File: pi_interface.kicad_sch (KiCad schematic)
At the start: 7 parts, among them J3 GPIO, U5 M24c64

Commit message: push forwards: clock muxing, filling in blanks
Finished off the ethernet section finally.
Sorted a solution to the 25M phy clocks required for ethercat
Connected CAN as per existing hardware (and fixed a bug in speed mode)
Sorted out bypassing for MCU
Added more thoughts on the external interfaces
Started on a 24V supply
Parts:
- added JP3: KJumper_2, TestPoint:TestPoint_2Pads_Pitch2.54mm_Drill0.8mm, symbol karl-parts:KJumper_2
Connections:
- net +5V: now also JP3.2 (B); no longer J3.2 (Pin_2), J3.4 (Pin_4), TP5.1
- new net 5VPI: J3.2 (Pin_2), J3.4 (Pin_4), JP3.1 (A), TP5.1
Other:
- note added: "A "proper" power hat supplies 3/5A at 5.1. We may want to be powered by the Pi, Or attempt to power it. Just be careful ok?"
- note added: "TODO * SPI? * UART? * SWD? (you can openocd on the pi and reprogram it on the fly? heh) * Let's say a UART _at least_ ? If you do this "right", you can stack it with my of my ADC hats and get a "HWS2" without putting any analog on this board at all... ==> Doesn't even have to stack, can just have the XMC as the "base" with a pi adc on top?"
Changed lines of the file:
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@@
+		)
+	)
+	(text "TODO\n* SPI?\n* UART?\n* SWD? (you can openocd on the pi and reprogram it on the fly? heh)\n* Let's say a UART _at least_ ?\n\nIf you do this \"right\", you can stack it with my of my ADC hats and get a \"HWS2\"\nwithout putting any analog on this board at all...\n\n==> Doesn't even have to stack, can just have the XMC as the \"base\" with a pi adc on top?"
+		(exclude_from_sim no)
+		(at 82.296 123.444 0)
+		(effects
+			(font
+				(size 2.54 2.54)
+			)
+			(justify left)
+		)
+	)
+	(text "A \"proper\" power hat supplies 3/5A at 5.1.\nWe may want to be powered by the Pi,\nOr attempt to power it.  Just be careful ok?"
+		(exclude_from_sim no)
+		(at 116.586 30.48 0)
+		(effects
+			(font
+				(size 1.27 1.27)
+			)
+			(justify left)
 		)
 	)
@@
 	(wire
 		(pts
+			(xy 134.62 25.4) (xy 139.7 25.4)
+		)
+		(stroke
+			(width 0)
+			(type default)
+		)
+	)
+	(wire
+		(pts
 			(xy 63.5 73.66) (xy 66.04 73.66)
 		)
@@
 	(wire
 		(pts
-			(xy 81.28 20.32) (xy 81.28 25.4)
+			(xy 81.28 17.78) (xy 81.28 25.4)
 		)
 		(stroke
@@
 		(pts
 			(xy 40.64 50.8) (xy 66.04 50.8)
+		)
+		(stroke
+			(width 0)
+			(type default)
+		)
+	)
+	(wire
+		(pts
+			(xy 127 25.4) (xy 129.54 25.4)
 		)
 		(stroke
@@
 		)
 	)
+	(global_label "5VPI"
+		(shape bidirectional)
+		(at 81.28 17.78 0)
+		(fields_autoplaced yes)
+		(effects
+			(font
+				(size 1.27 1.27)
+			)
+			(justify left)
+		)
+		(property "Intersheetrefs" "${INTERSHEET_REFS}"
+			(at 89.5494 17.78 0)
+			(hide yes)
+			(show_name no)
+			(do_not_autoplace no)
+			(effects
+				(font
+					(size 1.27 1.27)
+				)
+				(justify left)
+			)
+		)
+	)
+	(global_label "5VPI"
+		(shape bidirectional)
+		(at 127 25.4 180)
+		(fields_autoplaced yes)
+		(effects
+			(font
+				(size 1.27 1.27)
+			)
+			(justify right)
+		)
+		(property "Intersheetrefs" "${INTERSHEET_REFS}"
+			(at 118.7306 25.4 0)
+			(hide yes)
+			(show_name no)
+			(do_not_autoplace no)
+			(effects
+				(font
+					(size 1.27 1.27)
+				)
+				(justify right)
+			)
+		)
+	)
 	(symbol
 		(lib_id "power:+5V")
-		(at 81.28 20.32 0)
+		(at 139.7 25.4 0)
 		(unit 1)
 		(body_style 1)
@@
 		(dnp no)
 		(property "Reference" "#PWR01"
-			(at 81.28 24.13 0)
+			(at 139.7 29.21 0)
 			(hide yes)
 			(show_name no)
@@
 		)
 		(property "Value" "+5V"
-			(at 81.6483 15.9956 0)
+			(at 140.0683 21.0756 0)
 			(show_name no)
 			(do_not_autoplace no)
@@
 		)
 		(property "Footprint" ""
-			(at 81.28 20.32 0)
+			(at 139.7 25.4 0)
 			(show_name no)
 			(do_not_autoplace no)
@@
 		)
 		(property "Datasheet" ""
-			(at 81.28 20.32 0)
+			(at 139.7 25.4 0)
 			(show_name no)
 			(do_not_autoplace no)
@@
 		)
 		(property "Description" "Power symbol creates a global label with name \"+5V\""
-			(at 81.28 20.32 0)
+			(at 139.7 25.4 0)
 			(hide yes)
 			(show_name no)
@@
 					(unit 1)
 				)
+			)
+		)
+	)
+	(symbol
+		(lib_id "karl-parts:KJumper_2")
+		(at 132.08 25.4 0)
+		(unit 1)
+		(body_style 1)
+		(exclude_from_sim no)
+		(in_bom yes)
+		(on_board yes)
+		(in_pos_files yes)
+		(dnp no)
+		(fields_autoplaced yes)
+		(property "Reference" "JP3"
+			(at 132.08 19.05 0)
+			(show_name no)
+			(do_not_autoplace no)
+			(effects
+				(font
+					(size 1.27 1.27)
+				)
+			)
+		)
+		(property "Value" "KJumper_2"
+			(at 132.08 21.59 0)
+			(show_name no)
+			(do_not_autoplace no)
+			(effects
+				(font
+					(size 1.27 1.27)
+				)
+			)
+		)
+		(property "Footprint" "TestPoint:TestPoint_2Pads_Pitch2.54mm_Drill0.8mm"
+			(at 132.08 25.4 0)
+			(hide yes)
+			(show_name no)
+			(do_not_autoplace no)
+			(effects
+				(font
+					(size 1.27 1.27)
+				)
+			)
+		)
+		(property "Datasheet" ""
+			(at 132.08 25.4 0)
+			(hide yes)
+			(show_name no)
+			(do_not_autoplace no)
+			(effects
+				(font
+					(size 1.27 1.27)
+				)
+			)
+		)
+		(property "Description" "Jumper, 2-pole, small symbol, open"
+			(at 132.08 25.4 0)
+			(hide yes)
+			(show_name no)
+			(do_not_autoplace no)
+			(effects
+				(font
+					(size 1.27 1.27)
+				)
+			)
+		)
+		(pin "2"
+		)
+		(pin "1"
+		)
+		(instances
+			(project "xmc-ecat-enet-twin"
+				(path "/f5c7c34d-e330-4aa5-be7e-80f0a3a977af/8a413513-9505-4930-8a63-18ba86ee9e3b"
+					(reference "JP3")
+					(unit 1)
+				)

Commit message: finish a 24V supply
went with a more modern one, plenty of room.  Should be pretty good now.
Went over and filled in a bunch of missing parts and things, cleaned up
as much as I could 0603 vs 0402 for most, updated some thigns to current
atomic part library.

still to go, the "pi" interface and some sort of spi/io interface?
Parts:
- removed C2: 100nF, Capacitor_SMD:C_0603_1608Metric, symbol karl-atomic-basic:KC0603_100nF
- added C25: 100nF, Capacitor_SMD:C_0402_1005Metric, symbol karl-atomic-basic:KC0402_100nF
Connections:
- net +3V3: now also C25.1; no longer JP1.2 (B)
- net GND: now also C25.2
- net at U5.7 (WP): no longer JP1.1 (A)

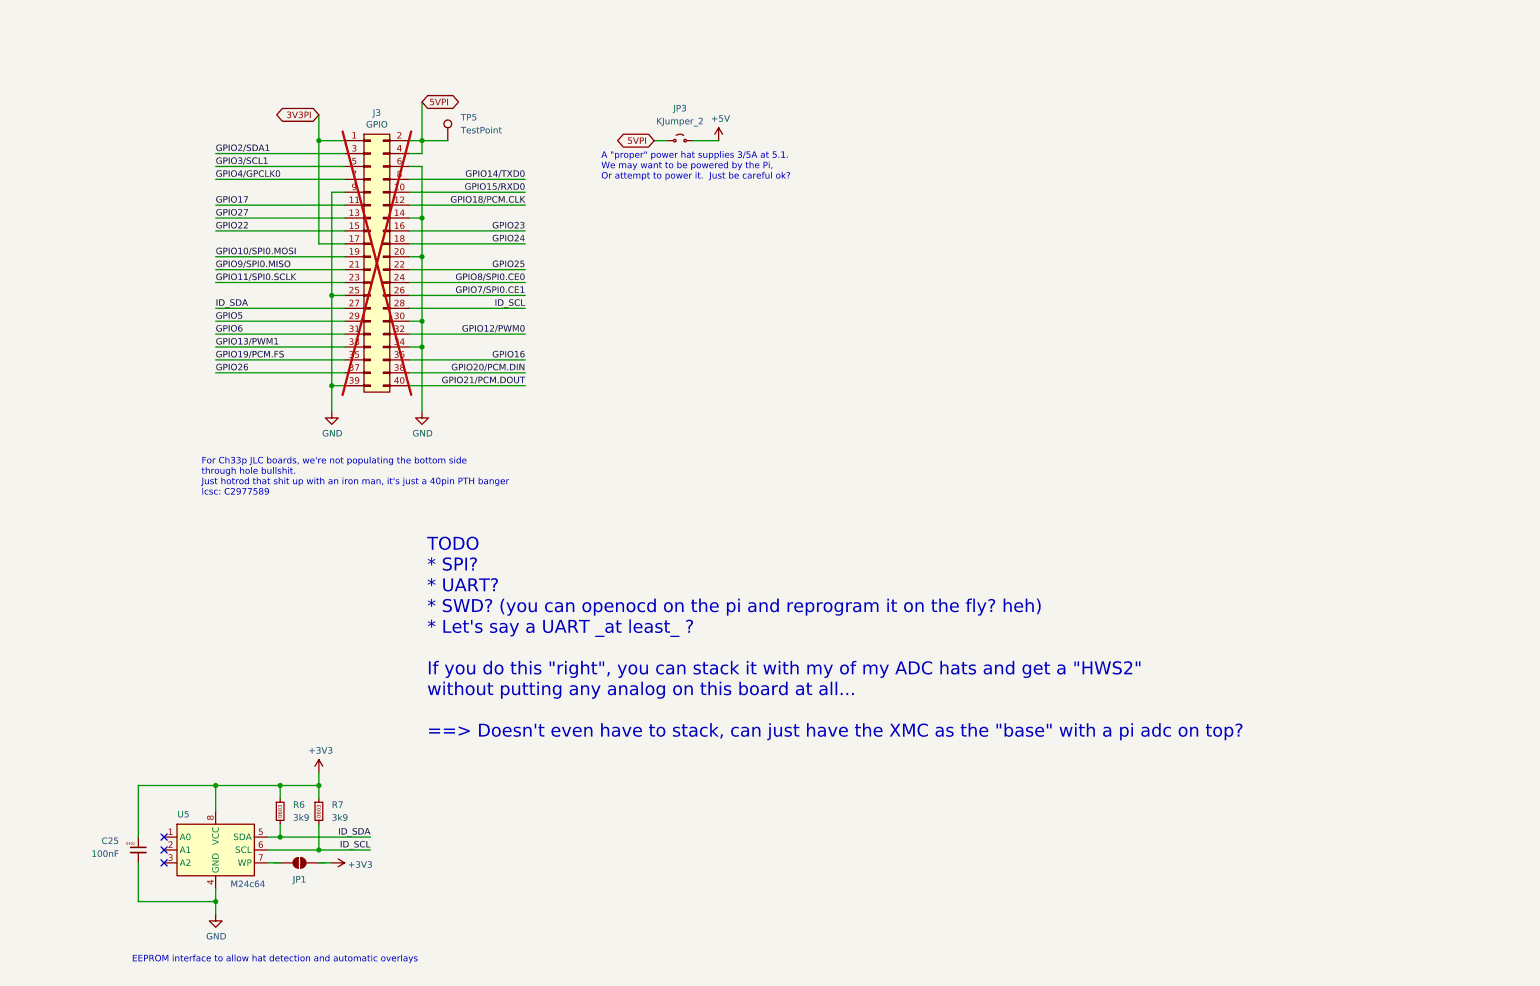
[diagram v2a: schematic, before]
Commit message: connect spi and uart to pi interface
we'll even have jumpers for being the hat or the baseboard for uart...

need to re-open modus to find new pins for i2c...
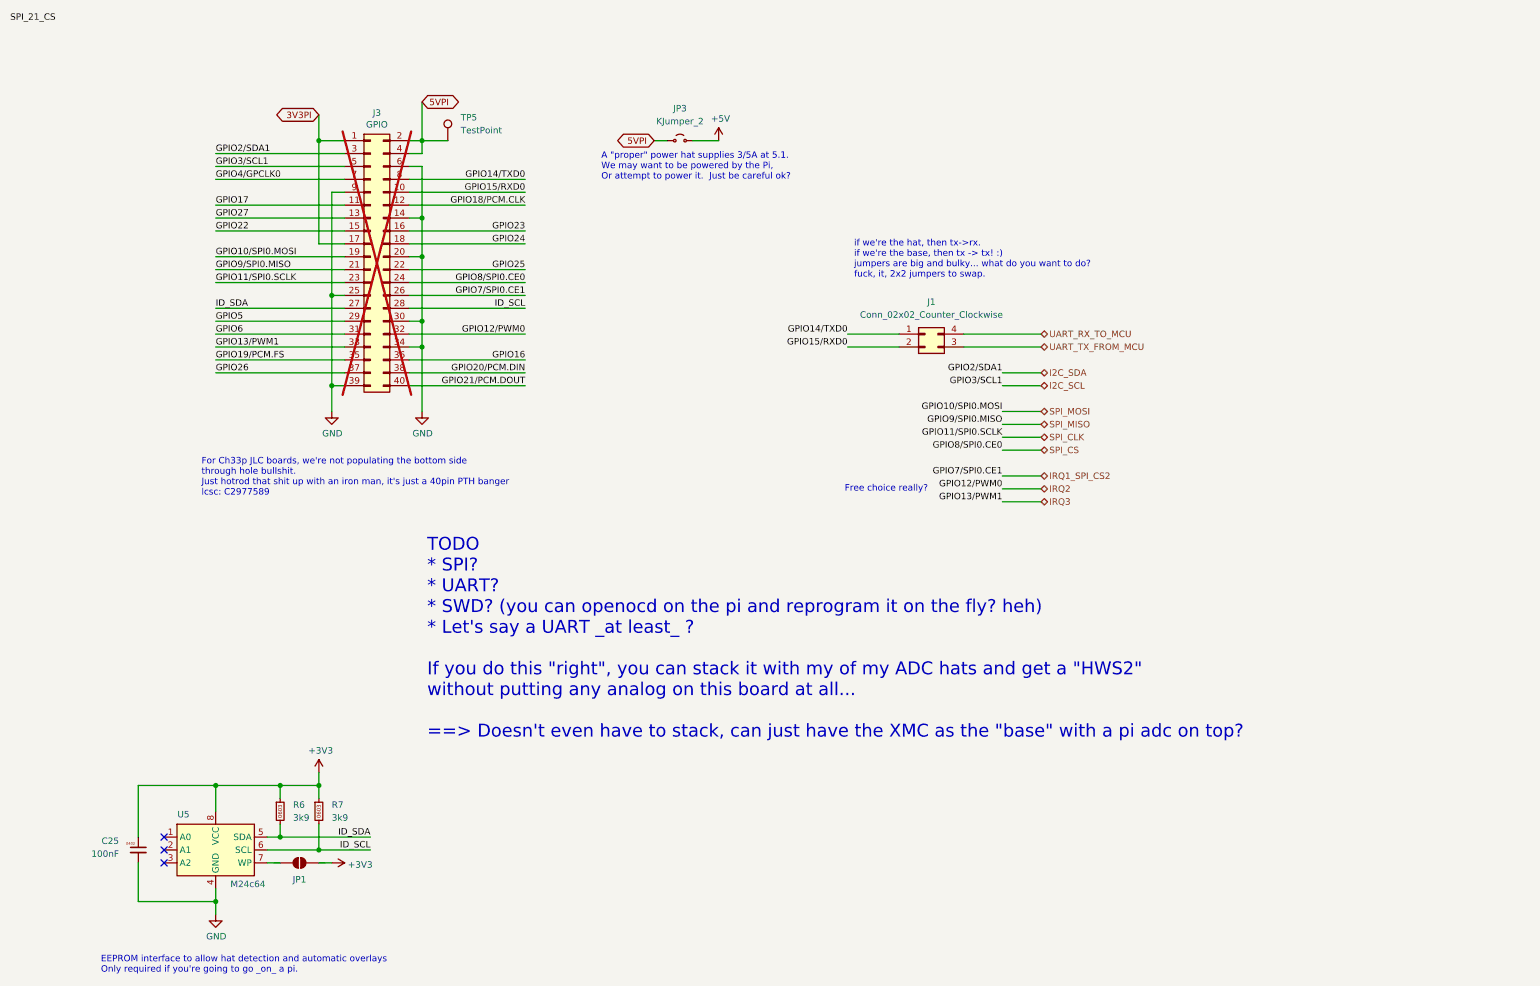
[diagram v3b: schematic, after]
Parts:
- added J1: Conn_02x02_Counter_Clockwise, Connector_PinHeader_2.54mm:PinHeader_2x02_P2.54mm_Vertical, symbol Connector_Generic:Conn_02x02_Counter_Clockwise
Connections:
- net GPIO14/TXD0: now also J1.1 (Pin_1)
- net GPIO15/RXD0: now also J1.2 (Pin_2)
- net GPIO10/SPI0.MOSI renamed SPI_MOSI
- net GPIO11/SPI0.SCLK renamed SPI_CLK
- net GPIO12/PWM0 renamed IRQ2
- net GPIO13/PWM1 renamed IRQ3
- net GPIO2/SDA1 renamed I2C_SDA
- net GPIO3/SCL1 renamed I2C_SCL
- net GPIO7/SPI0.CE1 renamed IRQ1_SPI_CS2
- net GPIO8/SPI0.CE0 renamed SPI_CS
- net GPIO9/SPI0.MISO renamed SPI_MISO
- new net UART_RX_TO_MCU: J1.4 (Pin_4)
- new net UART_TX_FROM_MCU: J1.3 (Pin_3)
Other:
- note added: "EEPROM interface to allow hat detection and automatic overlays Only required if you're going to go _on_ a pi."
- note added: "Free choice really?"
- note added: "if we're the hat, then tx->rx. if we're the base, then tx -> tx! :) jumpers are big and bulky... what do you want to do? fuck, it, 2x2 jumpers to swap."
- note removed: "EEPROM interface to allow hat detection and automatic overlays"
